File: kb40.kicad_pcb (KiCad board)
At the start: 2 copper layers, 144.3 x 103.7 mm, 84 parts, among them J1 TRRS, J2 OLED, SW1 Choc, SW10 Choc, SW11 Choc, SW12 Choc, SW13 Choc, SW14 Choc, SW15 Choc, SW16 Choc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

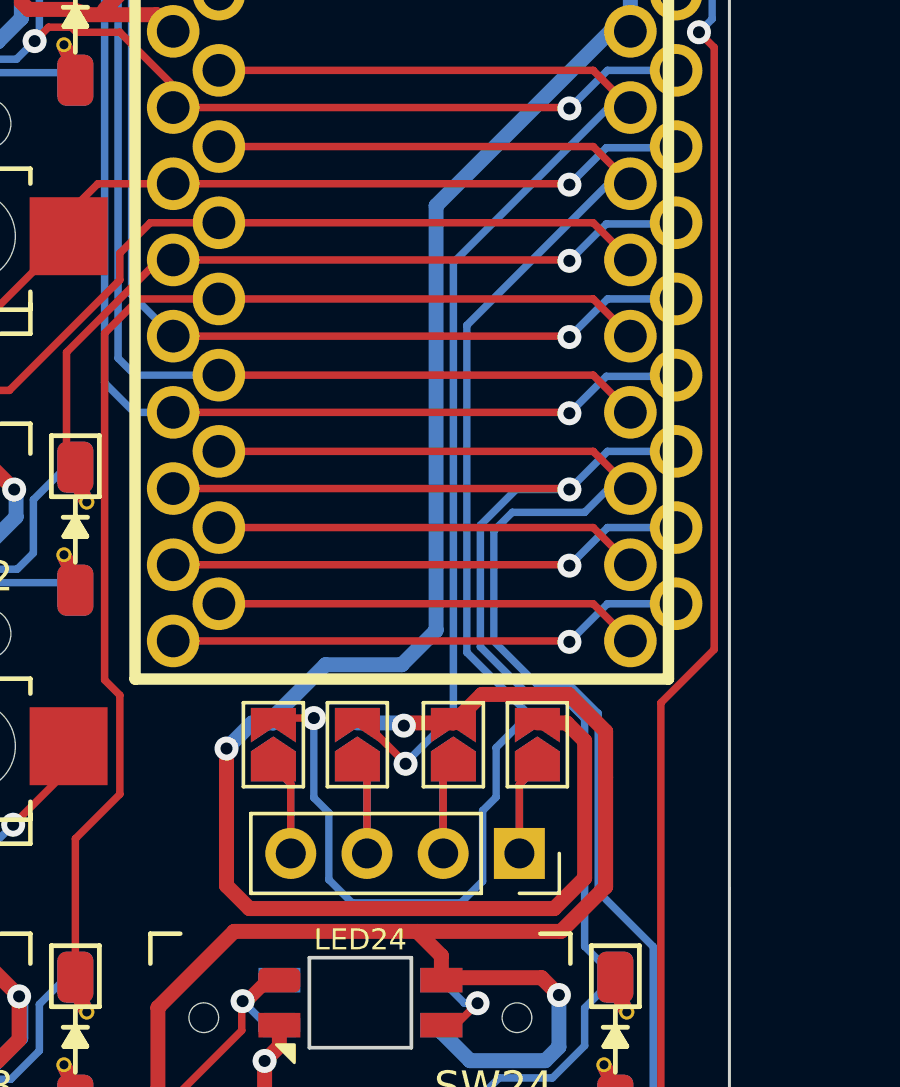
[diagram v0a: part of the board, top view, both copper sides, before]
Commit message: fix i2c and generate gerbers
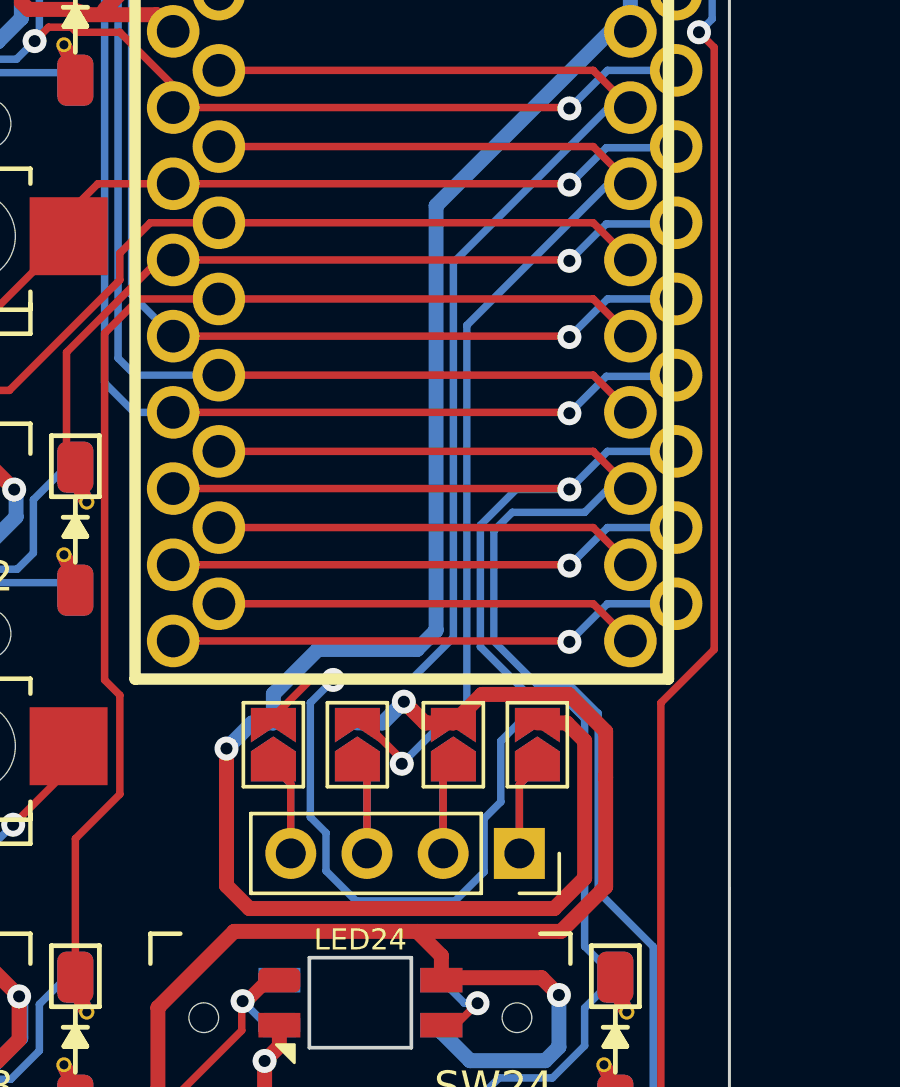
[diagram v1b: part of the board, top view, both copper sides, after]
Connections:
- JP1 pad 2: SCL -> SDA
- JP2 pad 2: SDA -> SCL
- JP7 pad 2: SDA -> SCL
- JP8 pad 2: SCL -> SDA
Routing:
- net SDA: track 42.0 -> 61.1 mm
- net SCL: track 55.0 -> 39.7 mm
- net VCC: track 963.9 -> 964.5 mm
